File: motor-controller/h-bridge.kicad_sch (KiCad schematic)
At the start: 0 parts

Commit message: Create H-Bridge schematic
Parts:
- added C3: 100nF, Capacitor_THT:C_Disc_D3.0mm_W2.0mm_P2.50mm, symbol GS_Capacitor_THT:C_THT_100nF
- added Q1, Q2, Q3, Q4: IRFZ44, Package_TO_SOT_THT:TO-220-3_Vertical, symbol GS_Transistors:MOSFET_N-Ch_60V_48A_23mR
- added Q5, Q6: VN2222L, Package_TO_SOT_THT:TO-92_Inline, symbol GS_Transistors:MOSFET_N-Ch_60V_0.23A_7500mR
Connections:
- new net GND: Q3.3 (S), Q4.3 (S), Q5.3 (D), Q6.3 (D)
- new net IN+: Q1.1 (G), Q4.1 (G), Q5.1 (S), Q6.2 (G)
- new net IN-: Q2.1 (G), Q3.1 (G), Q5.2 (G), Q6.1 (S)
- new net MOTOR+: C3.1, Q1.3 (S), Q3.2 (D)
- new net MOTOR-: C3.2, Q2.3 (S), Q4.2 (D)
- new net VDD: Q1.2 (D), Q2.2 (D)
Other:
- company: (none) -> Team 5
- title: (none) -> H-Bridge

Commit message: Finish optocoupler and gate-driver
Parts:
- renumbered C3 to C4, Q3 to Q10, Q2 to Q11, Q4 to Q12, Q5 to Q7, Q6 to Q8, Q1 to Q9

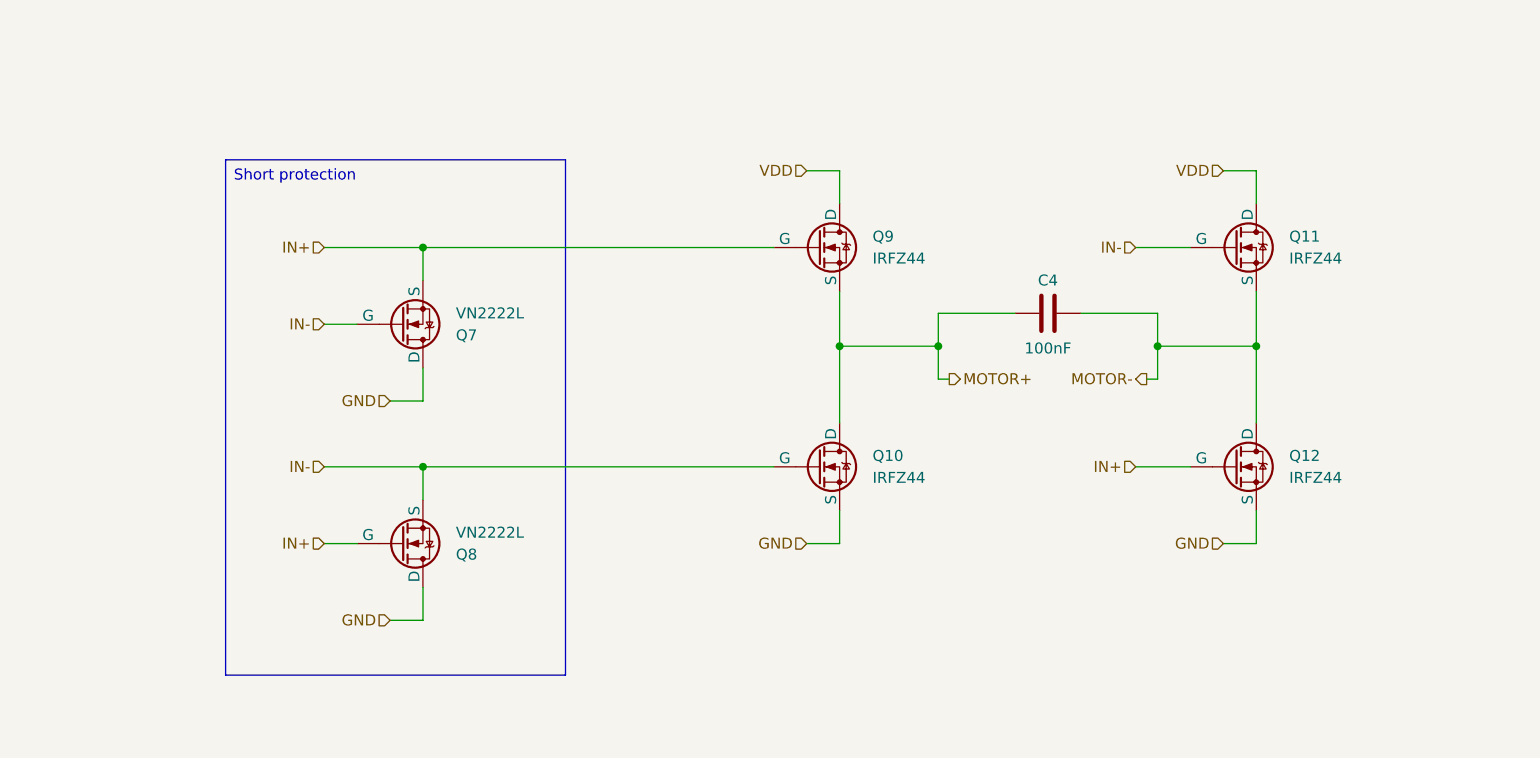
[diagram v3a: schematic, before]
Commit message: Change h-bridge design to newer version
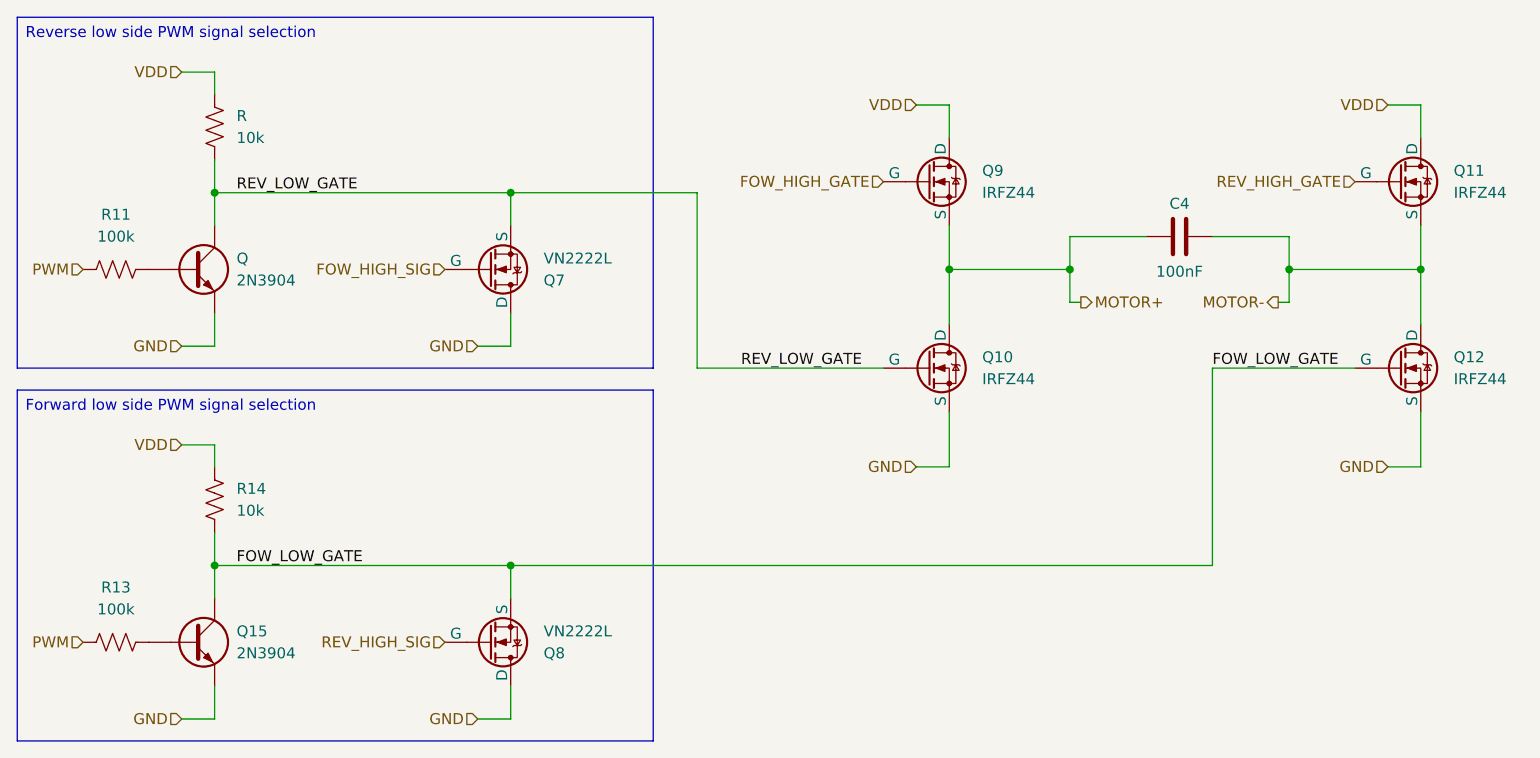
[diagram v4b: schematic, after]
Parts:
- added Q, Q15: 2N3904, Package_TO_SOT_THT:TO-92_Inline, symbol GS_Transistors:BJT_NPN_40V_200mA
- added R, R14: 10k, Resistor_THT:R_Axial_DIN0309_L9.0mm_D3.2mm_P12.70mm_Horizontal, symbol GS_Resistor_THT:R_250mW
- added R11, R13: 100k, Resistor_THT:R_Axial_DIN0309_L9.0mm_D3.2mm_P12.70mm_Horizontal, symbol GS_Resistor_THT:R_250mW
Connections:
- net GND: now also Q.E, Q15.E
- net VDD: now also R.1, R14.1
- removed net IN+: Q12.1 (G), Q7.1 (S), Q8.2 (G), Q9.1 (G)
- removed net IN-: Q10.1 (G), Q11.1 (G), Q7.2 (G), Q8.1 (S)
- new net: Q.B, R11.2
- new net: Q15.B, R13.2
- new net FOW_HIGH_GATE: Q9.1 (G)
- new net FOW_HIGH_SIG: Q7.2 (G)
- new net FOW_LOW_GATE: Q12.1 (G), Q15.C, Q8.1 (S), R14.2
- new net PWM: R11.1, R13.1
- new net REV_HIGH_GATE: Q11.1 (G)
- new net REV_HIGH_SIG: Q8.2 (G)
- new net REV_LOW_GATE: Q.C, Q10.1 (G), Q7.1 (S), R.2
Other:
- moved on the sheet: C4, Q10, Q11, Q12, Q7, Q8, Q9

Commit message: Fix some ERC issues
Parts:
- renumbered C4 to C13, Q8 to Q10, Q9 to Q3, Q11 to Q4, Q to Q5, Q7 to Q6, Q10 to Q7, Q12 to Q8, Q15 to Q9, R to R5, R11 to R6, R14 to R7, R13 to R8
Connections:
- net FOW_LOW_GATE: now also Q9.3 (C); no longer Q9.C
- net REV_LOW_GATE: now also Q5.3 (C); no longer Q5.C
- net at R6.2: now also Q5.2 (B); no longer Q5.B
- net at R8.2: now also Q9.2 (B); no longer Q9.B
- net GND renamed GNDPWR
- net GNDPWR: now also Q5.1 (E), Q9.1 (E); no longer Q5.E, Q9.E
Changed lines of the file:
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@@
 	(title_block
 		(title "H-Bridge")
-		(date "2025-06-05")
+		(date "2025-06-14")
 		(rev "A")
 		(company "Team 5")
@@
 		)
 	)
-	(hierarchical_label "GND"
+	(hierarchical_label "GNDPWR"
 		(shape input)
 		(at 175.26 68.58 180)
@@
 		)
 	)
-	(hierarchical_label "GND"
+	(hierarchical_label "GNDPWR"
 		(shape input)
 		(at 69.85 97.79 180)
@@
 		)
 	)
-	(hierarchical_label "GND"
+	(hierarchical_label "GNDPWR"
 		(shape input)
 		(at 35.56 97.79 180)
@@
 		)
 	)
-	(hierarchical_label "GND"
+	(hierarchical_label "GNDPWR"
 		(shape input)
 		(at 35.56 54.61 180)
@@
 		)
 	)
-	(hierarchical_label "GND"
+	(hierarchical_label "GNDPWR"
 		(shape input)
 		(at 69.85 54.61 180)
@@
 		)
 	)
-	(hierarchical_label "GND"
+	(hierarchical_label "GNDPWR"
 		(shape input)
 		(at 120.65 68.58 180)
@@
 		(on_board yes)
 		(dnp no)
-		(property "Reference" "Q10"
+		(property "Reference" "Q7"
 			(at 128.27 55.8799 0)
 			(effects
@@
 			(project "motor-controller"
 				(path "/3cf627b4-179f-4b19-ad57-a5207e12b14c/4e94ea2c-a108-4be2-8ee4-b6e71c617b37"
-					(reference "Q6")
+					(reference "Q15")
 					(unit 1)
 				)
 				(path "/3cf627b4-179f-4b19-ad57-a5207e12b14c/8bf0a1e8-4227-49ee-854f-9e27e5e507a9"
-					(reference "Q10")
+					(reference "Q7")
 					(unit 1)
 				)
@@
 		(dnp no)
 		(fields_autoplaced yes)
-		(property "Reference" "Q11"
+		(property "Reference" "Q4"
 			(at 182.88 34.2899 0)
 			(effects
@@
 			(project "motor-controller"
 				(path "/3cf627b4-179f-4b19-ad57-a5207e12b14c/4e94ea2c-a108-4be2-8ee4-b6e71c617b37"
-					(reference "Q14")
+					(reference "Q12")
 					(unit 1)
 				)
 				(path "/3cf627b4-179f-4b19-ad57-a5207e12b14c/8bf0a1e8-4227-49ee-854f-9e27e5e507a9"
-					(reference "Q11")
+					(reference "Q4")
 					(unit 1)
 				)
@@
 		(dnp no)
 		(fields_autoplaced yes)
-		(property "Reference" "Q12"
+		(property "Reference" "Q8"
 			(at 182.88 55.8799 0)
 			(effects
@@
 				)
 				(path "/3cf627b4-179f-4b19-ad57-a5207e12b14c/8bf0a1e8-4227-49ee-854f-9e27e5e507a9"
-					(reference "Q12")
+					(reference "Q8")
 					(unit 1)
 				)
@@
 		(dnp no)
 		(fields_autoplaced yes)
-		(property "Reference" "R11"
+		(property "Reference" "R6"
 			(at 27.94 39.37 90)
 			(effects
@@
 				)
 				(path "/3cf627b4-179f-4b19-ad57-a5207e12b14c/8bf0a1e8-4227-49ee-854f-9e27e5e507a9"
-					(reference "R11")
+					(reference "R6")
 					(unit 1)
 				)
@@
 		(dnp no)
 		(fields_autoplaced yes)
-		(property "Reference" "R13"
+		(property "Reference" "R8"
 			(at 27.94 82.55 90)
 			(effects
@@
 				)
 				(path "/3cf627b4-179f-4b19-ad57-a5207e12b14c/8bf0a1e8-4227-49ee-854f-9e27e5e507a9"
-					(reference "R13")
+					(reference "R8")
 					(unit 1)
 				)
@@
 		(dnp no)
 		(fields_autoplaced yes)
-		(property "Reference" "Q"
+		(property "Reference" "Q5"
 			(at 41.91 44.4499 0)
 			(effects
@@
 			)
 		)
-		(pin "C"
-		)
-		(pin "E"
-		)
-		(pin "B"
+		(pin "1"
+		)
+		(pin "2"
+		)
+		(pin "3"
 		)
 		(instances
 			(project "motor-controller"
 				(path "/3cf627b4-179f-4b19-ad57-a5207e12b14c/4e94ea2c-a108-4be2-8ee4-b6e71c617b37"
-					(reference "Q1")
+					(reference "Q13")
+					(unit 1)
+				)
+				(path "/3cf627b4-179f-4b19-ad57-a5207e12b14c/8bf0a1e8-4227-49ee-854f-9e27e5e507a9"
+					(reference "Q5")
 					(unit 1)
 				)
@@
 		(dnp no)
 		(fields_autoplaced yes)
-		(property "Reference" "Q15"
+		(property "Reference" "Q9"
 			(at 41.91 87.6299 0)
 			(effects
@@
 			)
 		)
-		(pin "C"
-		)
-		(pin "E"
-		)
-		(pin "B"
+		(pin "1"
+		)
+		(pin "3"
+		)
+		(pin "2"
 		)
 		(instances
 			(project "motor-controller"
 				(path "/3cf627b4-179f-4b19-ad57-a5207e12b14c/4e94ea2c-a108-4be2-8ee4-b6e71c617b37"
-					(reference "Q2")
+					(reference "Q17")
 					(unit 1)
 				)
 				(path "/3cf627b4-179f-4b19-ad57-a5207e12b14c/8bf0a1e8-4227-49ee-854f-9e27e5e507a9"
-					(reference "Q15")
+					(reference "Q9")
 					(unit 1)
 				)
@@
 		(on_board yes)
 		(dnp no)
-		(property "Reference" "C4"
+		(property "Reference" "C13"
 			(at 151.13 38.1 90)
 			(effects
@@
 			(project "motor-controller"
 				(path "/3cf627b4-179f-4b19-ad57-a5207e12b14c/4e94ea2c-a108-4be2-8ee4-b6e71c617b37"
-					(reference "C10")
+					(reference "C14")
 					(unit 1)
 				)
 				(path "/3cf627b4-179f-4b19-ad57-a5207e12b14c/8bf0a1e8-4227-49ee-854f-9e27e5e507a9"
-					(reference "C4")
+					(reference "C13")
 					(unit 1)
 				)
@@
 		(dnp no)
 		(fields_autoplaced yes)
-		(property "Reference" "Q7"
+		(property "Reference" "Q6"
 			(at 77.47 46.9901 0)
 			(effects
@@
 			(project "motor-controller"
 				(path "/3cf627b4-179f-4b19-ad57-a5207e12b14c/4e94ea2c-a108-4be2-8ee4-b6e71c617b37"
-					(reference "Q3")
+					(reference "Q14")
 					(unit 1)
 				)
 				(path "/3cf627b4-179f-4b19-ad57-a5207e12b14c/8bf0a1e8-4227-49ee-854f-9e27e5e507a9"
-					(reference "Q7")
+					(reference "Q6")
 					(unit 1)
 				)
@@
 		(dnp no)
 		(fields_autoplaced yes)
-		(property "Reference" "Q9"
+		(property "Reference" "Q3"
 			(at 128.27 34.2899 0)
 			(effects
@@
 			(project "motor-controller"
 				(path "/3cf627b4-179f-4b19-ad57-a5207e12b14c/4e94ea2c-a108-4be2-8ee4-b6e71c617b37"
-					(reference "Q5")
+					(reference "Q11")
 					(unit 1)
 				)
 				(path "/3cf627b4-179f-4b19-ad57-a5207e12b14c/8bf0a1e8-4227-49ee-854f-9e27e5e507a9"
-					(reference "Q9")
+					(reference "Q3")
 					(unit 1)
 				)
@@
 		(on_board yes)
 		(dnp no)
-		(property "Reference" "R"
+		(property "Reference" "R5"
 			(at 41.91 27.9399 0)
 			(effects
@@
 			(project "motor-controller"
 				(path "/3cf627b4-179f-4b19-ad57-a5207e12b14c/4e94ea2c-a108-4be2-8ee4-b6e71c617b37"
-					(reference "R15")
+					(reference "R9")
+					(unit 1)
+				)
+				(path "/3cf627b4-179f-4b19-ad57-a5207e12b14c/8bf0a1e8-4227-49ee-854f-9e27e5e507a9"
+					(reference "R5")
 					(unit 1)
 				)
@@
 		(dnp no)
 		(fields_autoplaced yes)
-		(property "Reference" "Q8"
+		(property "Reference" "Q10"
 			(at 77.47 90.1701 0)
 			(effects
@@
 			(project "motor-controller"
 				(path "/3cf627b4-179f-4b19-ad57-a5207e12b14c/4e94ea2c-a108-4be2-8ee4-b6e71c617b37"
-					(reference "Q4")
+					(reference "Q18")
 					(unit 1)
 				)
 				(path "/3cf627b4-179f-4b19-ad57-a5207e12b14c/8bf0a1e8-4227-49ee-854f-9e27e5e507a9"
-					(reference "Q8")
+					(reference "Q10")
 					(unit 1)
 				)
@@
 		(on_board yes)
 		(dnp no)
-		(property "Reference" "R14"
+		(property "Reference" "R7"
 			(at 41.91 71.1199 0)
 			(effects
@@
 			(project "motor-controller"
 				(path "/3cf627b4-179f-4b19-ad57-a5207e12b14c/4e94ea2c-a108-4be2-8ee4-b6e71c617b37"
-					(reference "R16")
+					(reference "R11")
 					(unit 1)
 				)
 				(path "/3cf627b4-179f-4b19-ad57-a5207e12b14c/8bf0a1e8-4227-49ee-854f-9e27e5e507a9"
-					(reference "R14")
-					(unit 1)
-				)
+					(reference "R7")
+					(unit 1)
+				)

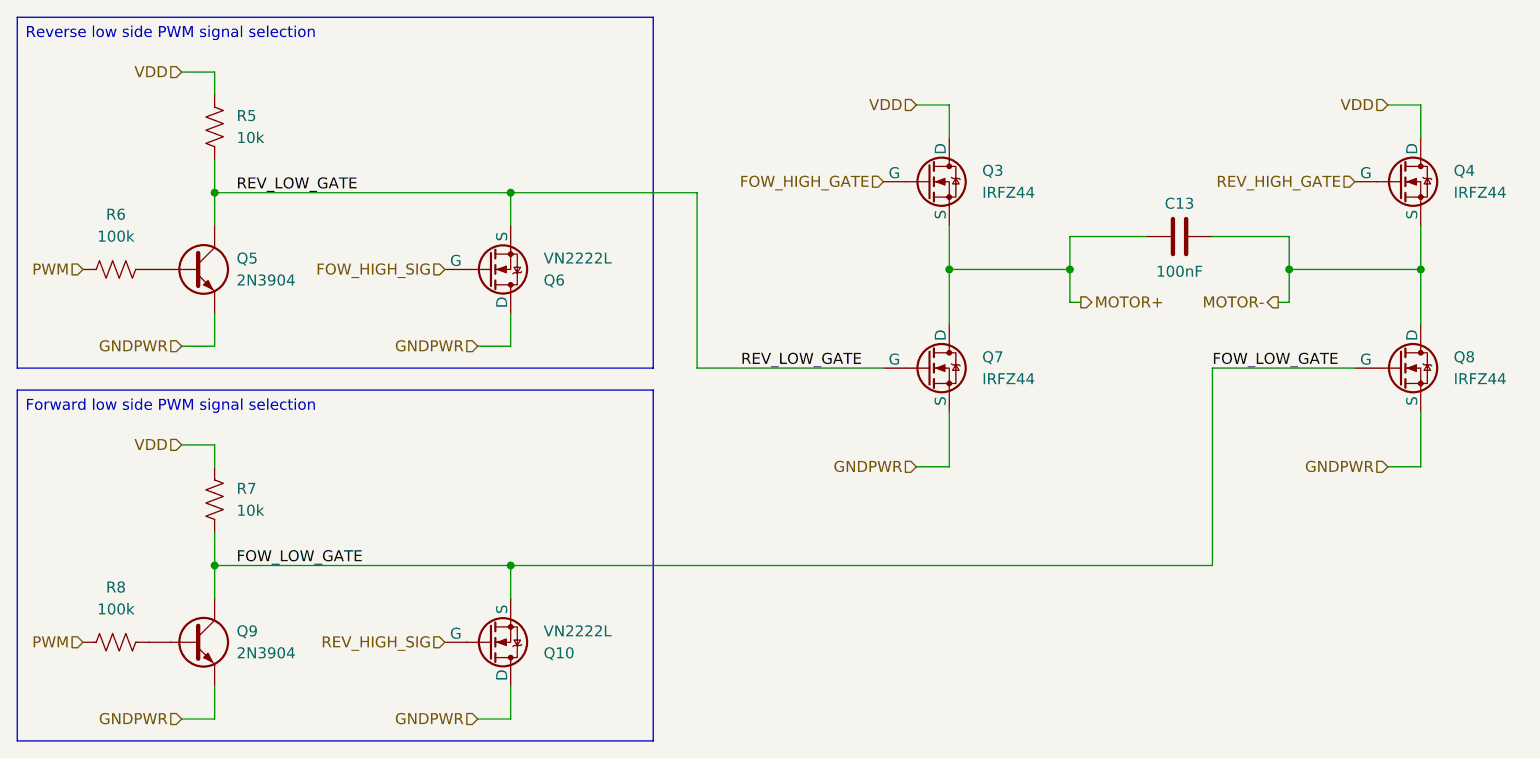
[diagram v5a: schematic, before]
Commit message: Update PWM signal selection to avoid an accidental resistor divider
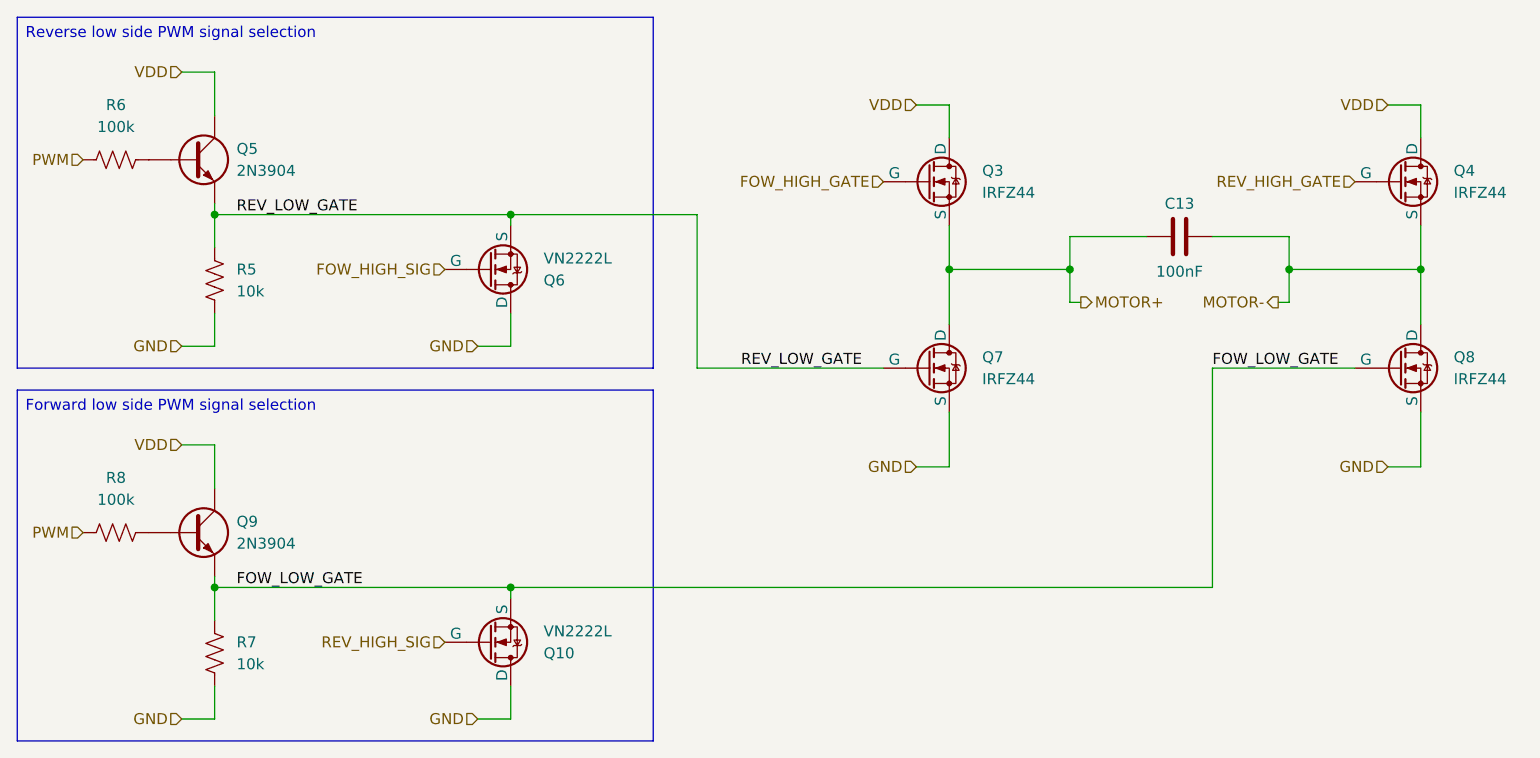
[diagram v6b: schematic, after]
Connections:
- net FOW_LOW_GATE: now also Q9.1 (E), R7.1; no longer Q9.3 (C), R7.2
- net REV_LOW_GATE: now also Q5.1 (E), R5.1; no longer Q5.3 (C), R5.2
- net VDD: now also Q5.3 (C), Q9.3 (C); no longer R5.1, R7.1
- net GNDPWR renamed GND
- net GND: now also R5.2, R7.2; no longer Q5.1 (E), Q9.1 (E)
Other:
- moved on the sheet: Q5, Q9, R5, R6, R7, R8
